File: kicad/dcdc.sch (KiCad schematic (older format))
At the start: 49 parts, among them Q1 IPA045N10N3G, Q2 IPA045N10N3G, Q8 IRF135B203, T6 MMBT3904, U1 LM5107, U3 TLV9001

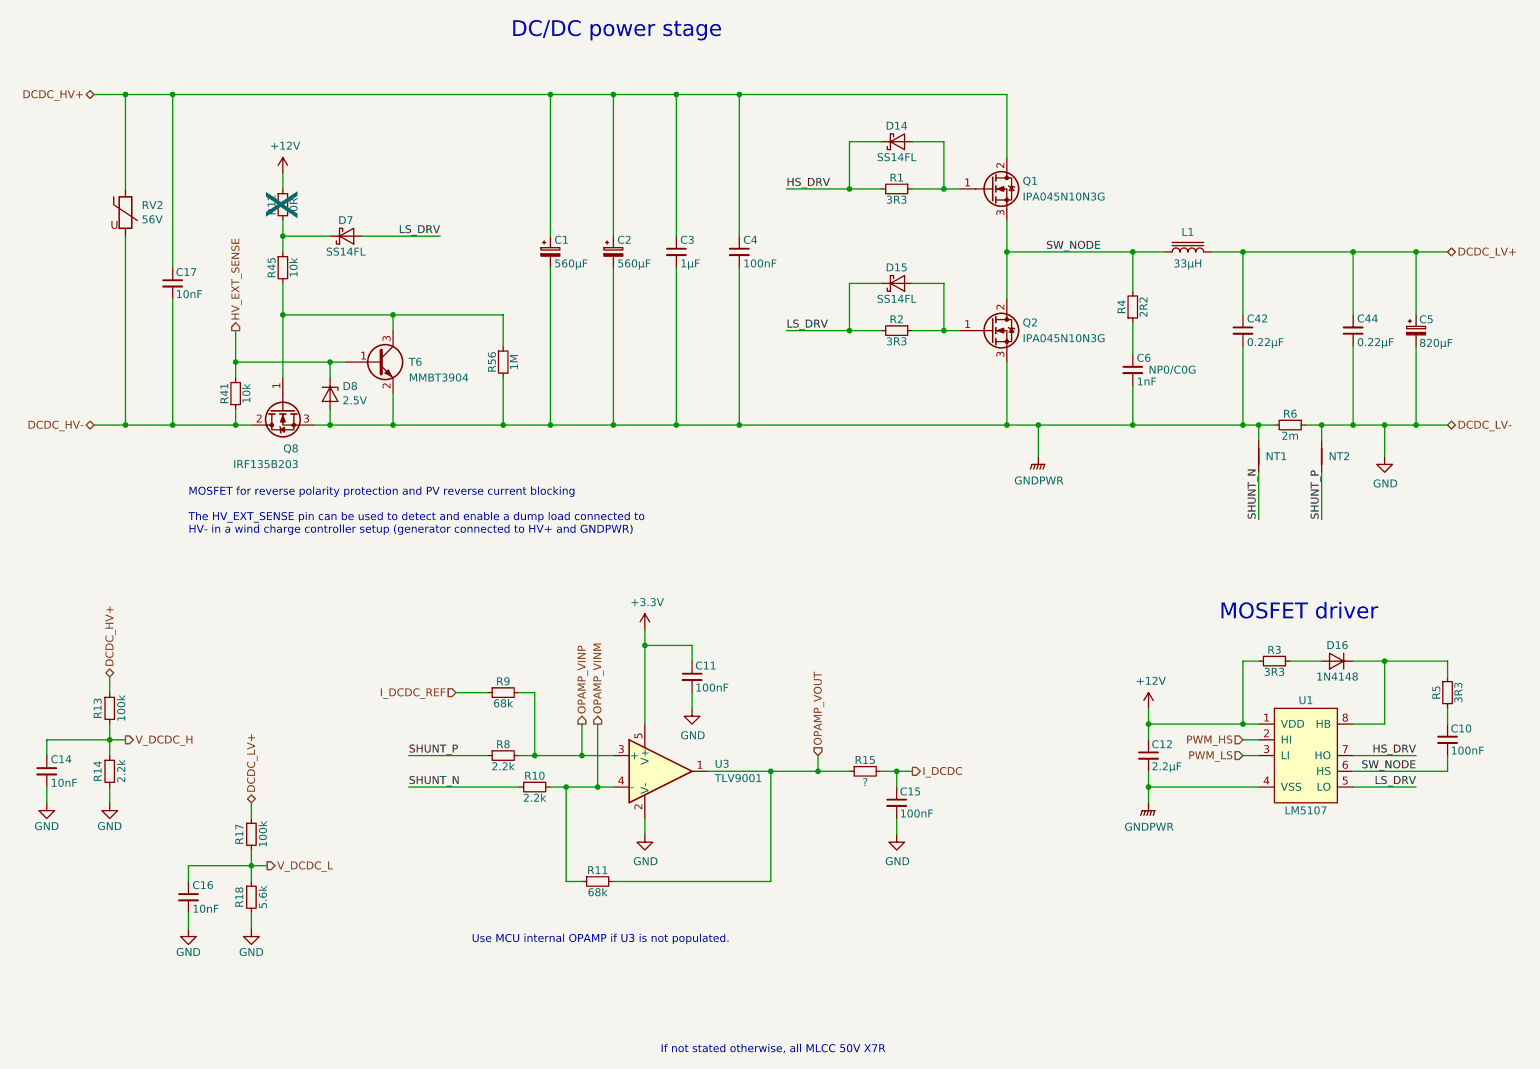
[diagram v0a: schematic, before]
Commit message: Fix errors after first prototype build-up
- Collision of capacitors with MOSFET clamps
- BOOT0 pin tied to GND
- Assignment of a few previously unasigned passives
- Add optional debug serial connector
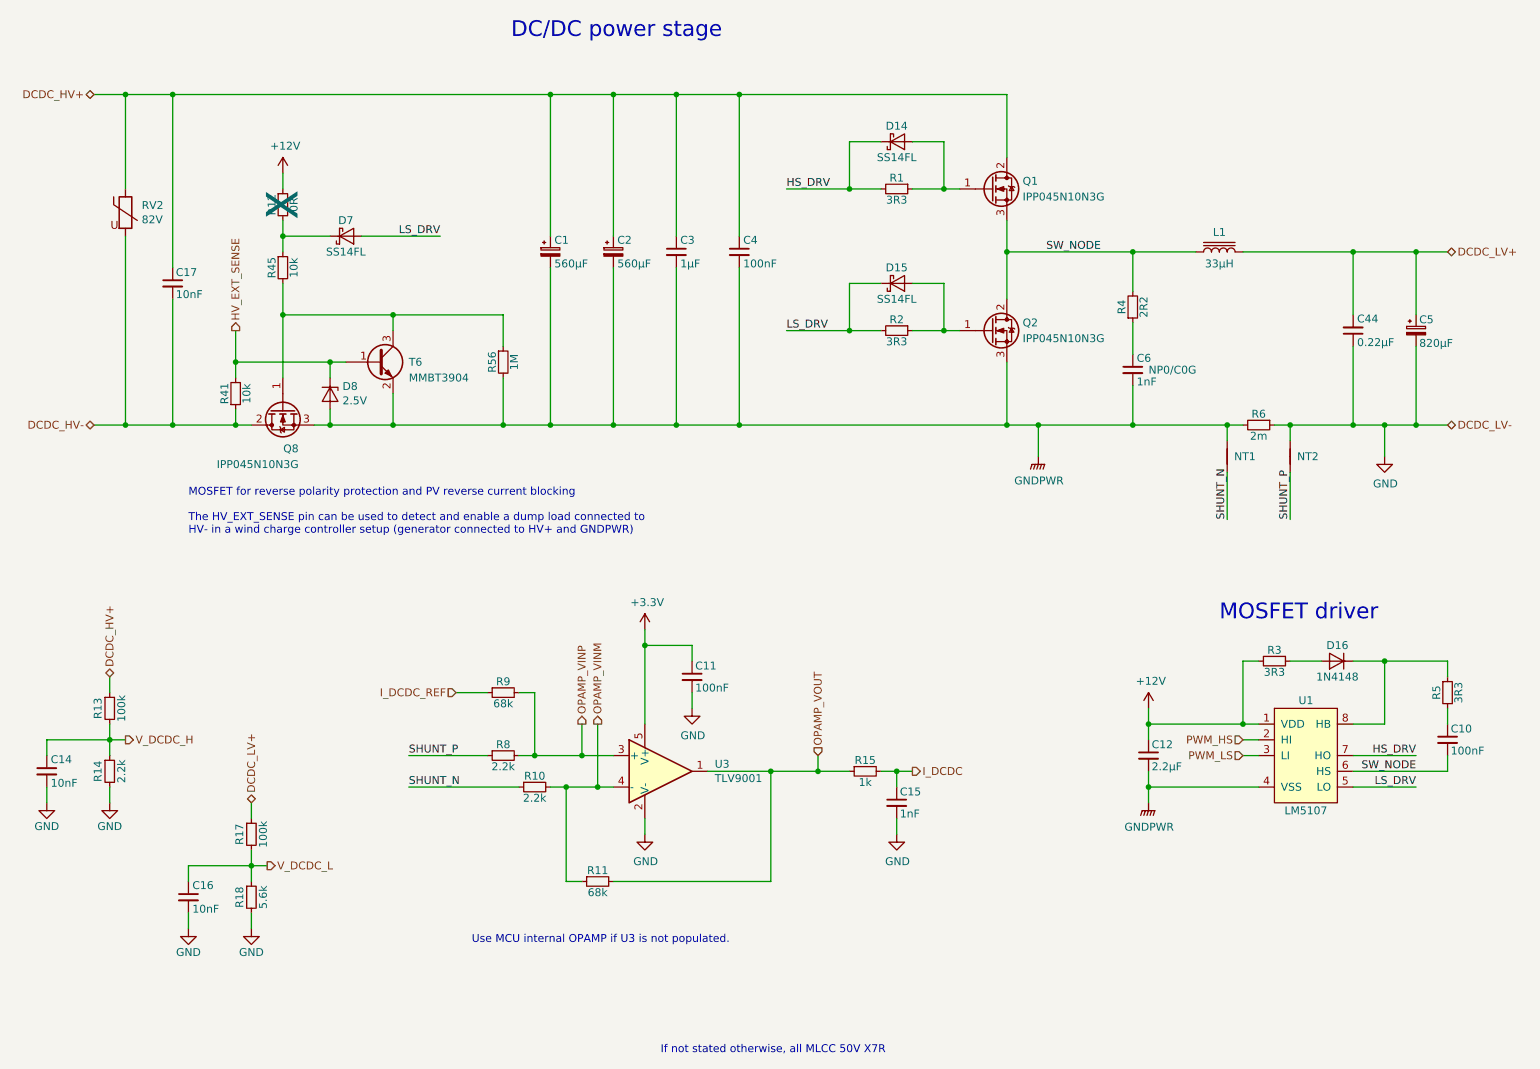
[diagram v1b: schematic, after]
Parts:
- removed C42: 0.22µF, Capacitor_THT:C_Rect_L7.2mm_W3.5mm_P5.00mm_FKS2_FKP2_MKS2_MKP2, symbol LibreSolar:C
- C15: value 100nF -> 1nF
- Q1, Q2: value IPA045N10N3G -> IPP045N10N3G; PartNumber IPA045N10N3G -> IPP045N10N3G
- Q8: value IRF135B203 -> IPP045N10N3G; PartNumber (none) -> IPP045N10N3G; Remarks 135V -> (none)
- R15: value ? -> 1k; PartNumber RC0603FR-07100KL -> RC0603FR-071KL
- RV2: value 56V -> 82V; PartNumber MOV-10D560K -> MOV-10D820K
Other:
- moved on the sheet: L1, NT1, NT2, R6
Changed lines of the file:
@@
 Sheet 2 5
 Title "MPPT 2420 RC"
-Date "2020-02-20"
-Rev "0.1"
+Date "2020-05-30"
+Rev "0.1.1"
 Comp "Libre Solar Technologies GmbH"
 Comment1 "Author: Martin Jäger"
@@
 L Device:L_Core_Iron L1
 U 1 1 58ACD441
-P 8450 2500
-F 0 "L1" V 8575 2500 50  0000 C CNN
-F 1 "33µH" V 8375 2500 50  0000 C CNN
-F 2 "LibreSolar:L-FERYSTER-DTMSS-27" V 8650 2500 50  0001 C CNN
-F 3 "" H 8450 2500 50  0001 C CNN
-F 4 "Feryster" H 1050 450 50  0001 C CNN "Manufacturer"
-F 5 "DTMSS-27/0,033/20-H" H 1050 450 50  0001 C CNN "PartNumber"
-F 6 "Feryster" H 8450 2500 60  0001 C CNN "Supplier"
-	1    8450 2500
+P 8650 2500
+F 0 "L1" V 8775 2500 50  0000 C CNN
+F 1 "33µH" V 8575 2500 50  0000 C CNN
+F 2 "LibreSolar:L-FERYSTER-DTMSS-27" V 8850 2500 50  0001 C CNN
+F 3 "" H 8650 2500 50  0001 C CNN
+F 4 "Feryster" H 1250 450 50  0001 C CNN "Manufacturer"
+F 5 "DTMSS-27/0,033/20-H" H 1250 450 50  0001 C CNN "PartNumber"
+F 6 "Feryster" H 8650 2500 60  0001 C CNN "Supplier"
+	1    8650 2500
 	0    -1   -1   0
 $EndComp
@@
 P 7200 2100
 F 0 "Q1" H 7400 2150 50  0000 L CNN
-F 1 "IPA045N10N3G" H 7400 2050 50  0000 L CNN
+F 1 "IPP045N10N3G" H 7400 2050 50  0000 L CNN
 F 2 "Package_TO_SOT_THT:TO-220-3_Vertical" H 7400 2200 50  0001 C CNN
 F 3 "" H 7200 2100 50  0001 C CNN
 F 4 "Infineon" H 1200 300 50  0001 C CNN "Manufacturer"
-F 5 "IPA045N10N3G" H 1200 300 50  0001 C CNN "PartNumber"
+F 5 "IPP045N10N3G" H 1200 300 50  0001 C CNN "PartNumber"
 	1    7200 2100
 	1    0    0    -1
@@
 P 7200 3000
 F 0 "Q2" H 7400 3050 50  0000 L CNN
-F 1 "IPA045N10N3G" H 7400 2950 50  0000 L CNN
+F 1 "IPP045N10N3G" H 7400 2950 50  0000 L CNN
 F 2 "Package_TO_SOT_THT:TO-220-3_Vertical" H 7400 3100 50  0001 C CNN
 F 3 "" H 7200 3000 50  0001 C CNN
 F 4 "Infineon" H 1200 500 50  0001 C CNN "Manufacturer"
-F 5 "IPA045N10N3G" H 1200 500 50  0001 C CNN "PartNumber"
+F 5 "IPP045N10N3G" H 1200 500 50  0001 C CNN "PartNumber"
 	1    7200 3000
 	1    0    0    -1
@@
 	4400 1500 4800 1500
 Wire Wire Line
-	8100 2500 8300 2500
-Wire Wire Line
-	8100 3600 8800 3600
+	8100 2500 8500 2500
 $Comp
 L Project:D_Schottky D15
@@
 L Project:R R6
 U 1 1 5C59CE9B
-P 9100 3600
+P 8900 3600
 AR Path="/58A68DC9/5C59CE9B" Ref="R6"  Part="1"
 AR Path="/5C45ED62/5C59CE9B" Ref="R?"  Part="1"
-F 0 "R6" V 9030 3600 50  0000 C CNN
-F 1 "2m" V 9170 3600 50  0000 C CNN
-F 2 "LibreSolar:R_Bourns_CRE2512" H 9100 3600 50  0001 C CNN
-F 3 "" H 9100 3600 50  0000 C CNN
-F 4 "Bourns" H 7350 -2300 50  0001 C CNN "Manufacturer"
-F 5 "CRE2512-FZ-R002E-3" H 7350 -2300 50  0001 C CNN "PartNumber"
-	1    9100 3600
+F 0 "R6" V 8830 3600 50  0000 C CNN
+F 1 "2m" V 8970 3600 50  0000 C CNN
+F 2 "LibreSolar:R_Bourns_CRE2512" H 8900 3600 50  0001 C CNN
+F 3 "" H 8900 3600 50  0000 C CNN
+F 4 "Bourns" H 7150 -2300 50  0001 C CNN "Manufacturer"
+F 5 "CRE2512-FZ-R002E-3" H 7150 -2300 50  0001 C CNN "PartNumber"
+	1    8900 3600
 	0    1    1    0
 $EndComp
@@
 P 6600 6000
 F 0 "C15" H 6620 6070 50  0000 L CNN
-F 1 "100nF" H 6620 5930 50  0000 L CNN
+F 1 "1nF" H 6620 5930 50  0000 L CNN
 F 2 "LibreSolar:C_0603_1608" H 6600 6000 50  0001 C CNN
 F 3 "" H 6600 6000 50  0000 C CNN
@@
 P 6400 5800
 F 0 "R15" V 6330 5800 50  0000 C CNN
-F 1 "?" V 6470 5800 50  0000 C CNN
+F 1 "1k" V 6470 5800 50  0000 C CNN
 F 2 "LibreSolar:R_0603_1608" H 6400 5800 50  0001 C CNN
 F 3 "" H 6400 5800 50  0000 C CNN
 F 4 "Yageo" H 850 3300 50  0001 C CNN "Manufacturer"
-F 5 "RC0603FR-07100KL" H 850 3300 50  0001 C CNN "PartNumber"
+F 5 "RC0603FR-071KL" H 850 3300 50  0001 C CNN "PartNumber"
 	1    6400 5800
 	0    -1   1    0
@@
 DCDC_HV-
 Wire Wire Line
-	8600 2500 8800 2500
-Wire Wire Line
 	2000 1500 2000 2600
 Connection ~ 2000 1500
@@
 I_DCDC_REF
 $Comp
-L LibreSolar:C C42
-U 1 1 5DAD80FB
-P 8800 3000
-F 0 "C42" H 8825 3075 50  0000 L CNN
-F 1 "0.22µF" H 8825 2925 50  0000 L CNN
-F 2 "Capacitor_THT:C_Rect_L7.2mm_W3.5mm_P5.00mm_FKS2_FKP2_MKS2_MKP2" H 8800 2800 50  0001 C CNN
-F 3 "" H 8825 3075 50  0001 C CNN
-F 4 "224J63" H 8800 3000 50  0001 C CNN "PartNumber"
-	1    8800 3000
-	1    0    0    -1
-$EndComp
-Wire Wire Line
-	8800 2900 8800 2500
-Connection ~ 8800 2500
-Wire Wire Line
-	8800 3100 8800 3600
-Connection ~ 8800 3600
-$Comp
 L Device:Varistor RV?
 U 1 1 5DC19B0F
@@
 AR Path="/58A68DC9/5DC19B0F" Ref="RV2"  Part="1"
 F 0 "RV2" H 1803 2296 50  0000 L CNN
-F 1 "56V" H 1803 2205 50  0000 L CNN
+F 1 "82V" H 1803 2205 50  0000 L CNN
 F 2 "Varistor:RV_Disc_D12mm_W4.3mm_P7.5mm" V 1630 2250 50  0001 C CNN
 F 3 "" H 1700 2250 50  0001 C CNN
 F 4 "Bourns" H 1700 2250 50  0001 C CNN "Manufacturer"
-F 5 "MOV-10D560K" H 1700 2250 50  0001 C CNN "PartNumber"
+F 5 "MOV-10D820K " H 1700 2250 50  0001 C CNN "PartNumber"
 	1    1700 2250
 	1    0    0    -1
@@
 AR Path="/5C5B9319/5DBB6507" Ref="Q?"  Part="1"
 F 0 "Q8" V 2950 3400 50  0000 L CNN
-F 1 "IRF135B203" V 3050 3400 50  0000 L CNN
+F 1 "IPP045N10N3G" V 3050 3400 50  0000 L CNN
 F 2 "Package_TO_SOT_THT:TO-220-3_Vertical" H 2900 3600 50  0001 C CNN
 F 3 "" H 2700 3500 50  0001 C CNN
 F 4 "Infineon" H 100 1050 50  0001 C CNN "Manufacturer"
-F 5 "135V" H 2700 3500 50  0001 C CNN "Remarks"
+F 5 "" H 2700 3500 50  0001 C CNN "Remarks"
+F 6 "IPP045N10N3G" H 2700 3500 50  0001 C CNN "PartNumber"
 	1    2700 3500
 	0    -1   1    0
@@
 	6300 3000 6500 3000
 Wire Wire Line
-	8800 3600 8900 3600
-Wire Wire Line
 	9500 3600 9700 3600
 Connection ~ 9500 3600
@@
 $EndComp
 Wire Wire Line
-	9200 3600 9300 3600
-Wire Wire Line
-	8800 2500 9500 2500
+	9000 3600 9100 3600
 Text HLabel 10100 3600 2    50   BiDi ~ 0
 DCDC_LV-
@@
 L Device:Net-Tie_2 NT1
 U 1 1 5E565394
-P 8900 3800
-F 0 "NT1" V 8900 3844 50  0000 L CNN
-F 1 "Net-Tie_2" V 8945 3844 50  0001 L CNN
-F 2 "NetTie:NetTie-2_SMD_Pad0.5mm" H 8900 3800 50  0001 C CNN
-F 3 "~" H 8900 3800 50  0001 C CNN
-	1    8900 3800
+P 8700 3800
+F 0 "NT1" V 8700 3844 50  0000 L CNN
+F 1 "Net-Tie_2" V 8745 3844 50  0001 L CNN
+F 2 "NetTie:NetTie-2_SMD_Pad0.5mm" H 8700 3800 50  0001 C CNN
+F 3 "~" H 8700 3800 50  0001 C CNN
+	1    8700 3800
 	0    1    1    0
 $EndComp
@@
 L Device:Net-Tie_2 NT2
 U 1 1 5E566B81
-P 9300 3800
-F 0 "NT2" V 9300 3844 50  0000 L CNN
-F 1 "Net-Tie_2" V 9345 3844 50  0001 L CNN
-F 2 "NetTie:NetTie-2_SMD_Pad0.5mm" H 9300 3800 50  0001 C CNN
-F 3 "~" H 9300 3800 50  0001 C CNN
-	1    9300 3800
+P 9100 3800
+F 0 "NT2" V 9100 3844 50  0000 L CNN
+F 1 "Net-Tie_2" V 9145 3844 50  0001 L CNN
+F 2 "NetTie:NetTie-2_SMD_Pad0.5mm" H 9100 3800 50  0001 C CNN
+F 3 "~" H 9100 3800 50  0001 C CNN
+	1    9100 3800
 	0    1    1    0
 $EndComp
 Wire Wire Line
-	9300 3700 9300 3600
-Connection ~ 9300 3600
-Wire Wire Line
-	9300 3600 9500 3600
-Wire Wire Line
-	8900 3700 8900 3600
-Connection ~ 8900 3600
-Wire Wire Line
-	8900 3600 9000 3600
-Wire Wire Line
-	8900 3900 8900 4200
-Wire Wire Line
-	9300 3900 9300 4200
-Text Label 9300 4200 1    50   ~ 0
+	9100 3700 9100 3600
+Connection ~ 9100 3600
+Wire Wire Line
+	9100 3600 9500 3600
+Wire Wire Line
+	8700 3700 8700 3600
+Connection ~ 8700 3600
+Wire Wire Line
+	8700 3600 8800 3600
+Wire Wire Line
+	8700 3900 8700 4200
+Wire Wire Line
+	9100 3900 9100 4200
+Text Label 9100 4200 1    50   ~ 0
 SHUNT_P
-Text Label 8900 4200 1    50   ~ 0
+Text Label 8700 4200 1    50   ~ 0
 SHUNT_N
 $Comp
@@
 Wire Wire Line
 	2700 2000 2700 2100
+Wire Wire Line
+	8100 3600 8700 3600
+Wire Wire Line
+	8800 2500 9500 2500
 $EndSCHEMATC

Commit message: Fix some references and part numbers
See issues #3, #5, #7, #8 and #9.
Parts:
- C14, C16: Manufacturer (none) -> Murata; PartNumber (none) -> GCM188R72A103KA37D; Remarks 50V, X7R -> 100V, X7R
- C15: Manufacturer Murata -> (none); PartNumber GRM188R71H104KA93D -> (none); Remarks (none) -> 50V, NP0/C0G
- R10, R14, R8: PartNumber RC0603FR-0710KL -> RC0603FR-072K2L
- R11, R9: PartNumber RC0603FR-0710KL -> RC0603FR-0768KL
- R12: PartNumber RC0603FR-0710KL -> RC0603FR-070RL
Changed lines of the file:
@@
 F 2 "LibreSolar:C_0603_1608" H 6600 6000 50  0001 C CNN
 F 3 "" H 6600 6000 50  0000 C CNN
-F 4 "Murata" H 1400 2100 50  0001 C CNN "Manufacturer"
-F 5 "GRM188R71H104KA93D" H 1400 2100 50  0001 C CNN "PartNumber"
+F 4 "50V, NP0/C0G" H 6600 6000 50  0001 C CNN "Remarks"
 	1    6600 6000
 	1    0    0    -1
@@
 F 2 "LibreSolar:C_0603_1608" H 2100 6400 50  0001 C CNN
 F 3 "" H 2125 6675 50  0000 C CNN
-F 4 "" H -4050 800 50  0001 C CNN "Manufacturer"
-F 5 "" H -4050 800 50  0001 C CNN "PartNumber"
-F 6 "50V, X7R" H 2100 6600 50  0001 C CNN "Remarks"
+F 4 "Murata" H -4050 800 50  0001 C CNN "Manufacturer"
+F 5 "GCM188R72A103KA37D" H -4050 800 50  0001 C CNN "PartNumber"
+F 6 "100V, X7R" H 2100 6600 50  0001 C CNN "Remarks"
 	1    2100 6600
 	1    0    0    -1
@@
 F 2 "LibreSolar:C_0603_1608" H 1200 5600 50  0001 C CNN
 F 3 "" H 1225 5875 50  0000 C CNN
-F 4 "" H -6100 0   50  0001 C CNN "Manufacturer"
-F 5 "" H -6100 0   50  0001 C CNN "PartNumber"
-F 6 "50V, X7R" H 1200 5800 50  0001 C CNN "Remarks"
+F 4 "Murata" H -6100 0   50  0001 C CNN "Manufacturer"
+F 5 "GCM188R72A103KA37D" H -6100 0   50  0001 C CNN "PartNumber"
+F 6 "100V, X7R" H 1200 5800 50  0001 C CNN "Remarks"
 	1    1200 5800
 	1    0    0    -1
@@
 F 3 "" H 1600 5800 50  0000 C CNN
 F 4 "Yageo" H -6050 0   50  0001 C CNN "Manufacturer"
-F 5 "RC0603FR-0710KL" H -6050 0   50  0001 C CNN "PartNumber"
+F 5 "RC0603FR-072K2L" H -6050 0   50  0001 C CNN "PartNumber"
 	1    1600 5800
 	1    0    0    -1
@@
 F 3 "" H 4100 5700 50  0000 C CNN
 F 4 "Yageo" H -1450 3200 50  0001 C CNN "Manufacturer"
-F 5 "RC0603FR-0710KL" H -1450 3200 50  0001 C CNN "PartNumber"
+F 5 "RC0603FR-072K2L" H -1450 3200 50  0001 C CNN "PartNumber"
 	1    4100 5700
 	0    -1   1    0
@@
 F 3 "" H 4100 5300 50  0000 C CNN
 F 4 "Yageo" H -1450 2800 50  0001 C CNN "Manufacturer"
-F 5 "RC0603FR-0710KL" H -1450 2800 50  0001 C CNN "PartNumber"
+F 5 "RC0603FR-0768KL" H -1450 2800 50  0001 C CNN "PartNumber"
 	1    4100 5300
 	0    -1   1    0
@@
 F 3 "" H 4300 5900 50  0000 C CNN
 F 4 "Yageo" H -1250 3400 50  0001 C CNN "Manufacturer"
-F 5 "RC0603FR-0710KL" H -1250 3400 50  0001 C CNN "PartNumber"
+F 5 "RC0603FR-072K2L" H -1250 3400 50  0001 C CNN "PartNumber"
 	1    4300 5900
 	0    -1   1    0
@@
 F 3 "" H 4700 6500 50  0000 C CNN
 F 4 "Yageo" H -850 4000 50  0001 C CNN "Manufacturer"
-F 5 "RC0603FR-0710KL" H -850 4000 50  0001 C CNN "PartNumber"
+F 5 "RC0603FR-0768KL" H -850 4000 50  0001 C CNN "PartNumber"
 	1    4700 6500
 	0    -1   1    0
@@
 F 3 "" H 2700 2200 50  0000 C CNN
 F 4 "Yageo" H 250 -3450 50  0001 C CNN "Manufacturer"
-F 5 "RC0603FR-0710KL" H 250 -3450 50  0001 C CNN "PartNumber"
+F 5 "RC0603FR-070RL" H 250 -3450 50  0001 C CNN "PartNumber"
 F 6 "X" V 2700 2200 200 0000 C CNN "DNP"
 	1    2700 2200

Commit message: Clean up BOM and add build folder for generated files
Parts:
- D14, D15, D7: Alternative Nexperia PMEG4010EGWX -> (none); Remarks (none) -> Alternative: Nexperia PMEG4010EGWX
- L1: Supplier Feryster -> (none)
- NT1, NT2: Config (none) -> +info
- U1: symbol Project:LM5107 -> LibreSolar:LM5107
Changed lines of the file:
@@
 F 4 "Feryster" H 1250 450 50  0001 C CNN "Manufacturer"
 F 5 "DTMSS-27/0,033/20-H" H 1250 450 50  0001 C CNN "PartNumber"
-F 6 "Feryster" H 8650 2500 60  0001 C CNN "Supplier"
+F 6 "" H 8650 2500 60  0001 C CNN "Supplier"
 	1    8650 2500
 	0    -1   -1   0
@@
 $EndComp
 $Comp
-L Project:LM5107 U1
+L LibreSolar:LM5107 U1
 U 1 1 58C054FE
 P 9200 5700
@@
 F 4 "ON Semiconductor" H 6600 2700 50  0001 C CNN "Manufacturer"
 F 5 "SS14FL" H 6600 2700 50  0001 C CNN "PartNumber"
-F 6 "Nexperia PMEG4010EGWX" H 6600 2700 50  0001 C CNN "Alternative"
+F 6 "" H 6600 2700 50  0001 C CNN "Alternative"
+F 7 "Alternative: Nexperia PMEG4010EGWX" H 6600 2700 50  0001 C CNN "Remarks"
 	1    6600 2700
 	1    0    0    -1
@@
 F 4 "ON Semiconductor" H 6600 1800 50  0001 C CNN "Manufacturer"
 F 5 "SS14FL" H 6600 1800 50  0001 C CNN "PartNumber"
-F 6 "Nexperia PMEG4010EGWX" H 6600 1800 50  0001 C CNN "Alternative"
+F 6 "" H 6600 1800 50  0001 C CNN "Alternative"
+F 7 "Alternative: Nexperia PMEG4010EGWX" H 6600 1800 50  0001 C CNN "Remarks"
 	1    6600 1800
 	1    0    0    -1
@@
 F 4 "ON Semiconductor" H 3100 2400 50  0001 C CNN "Manufacturer"
 F 5 "SS14FL" H 3100 2400 50  0001 C CNN "PartNumber"
-F 6 "Nexperia PMEG4010EGWX" H 3100 2400 50  0001 C CNN "Alternative"
+F 6 "" H 3100 2400 50  0001 C CNN "Alternative"
+F 7 "Alternative: Nexperia PMEG4010EGWX" H 3100 2400 50  0001 C CNN "Remarks"
 	1    3100 2400
 	1    0    0    -1
@@
 F 2 "NetTie:NetTie-2_SMD_Pad0.5mm" H 8700 3800 50  0001 C CNN
 F 3 "~" H 8700 3800 50  0001 C CNN
+F 4 "+info" H 8700 3800 50  0001 C CNN "Config"
 	1    8700 3800
 	0    1    1    0
@@
 F 2 "NetTie:NetTie-2_SMD_Pad0.5mm" H 9100 3800 50  0001 C CNN
 F 3 "~" H 9100 3800 50  0001 C CNN
+F 4 "+info" H 9100 3800 50  0001 C CNN "Config"
 	1    9100 3800
 	0    1    1    0
